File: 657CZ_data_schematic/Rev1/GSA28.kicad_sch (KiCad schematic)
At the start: 3 parts, among them J281P DA15_Socket, J281R DA15_Socket

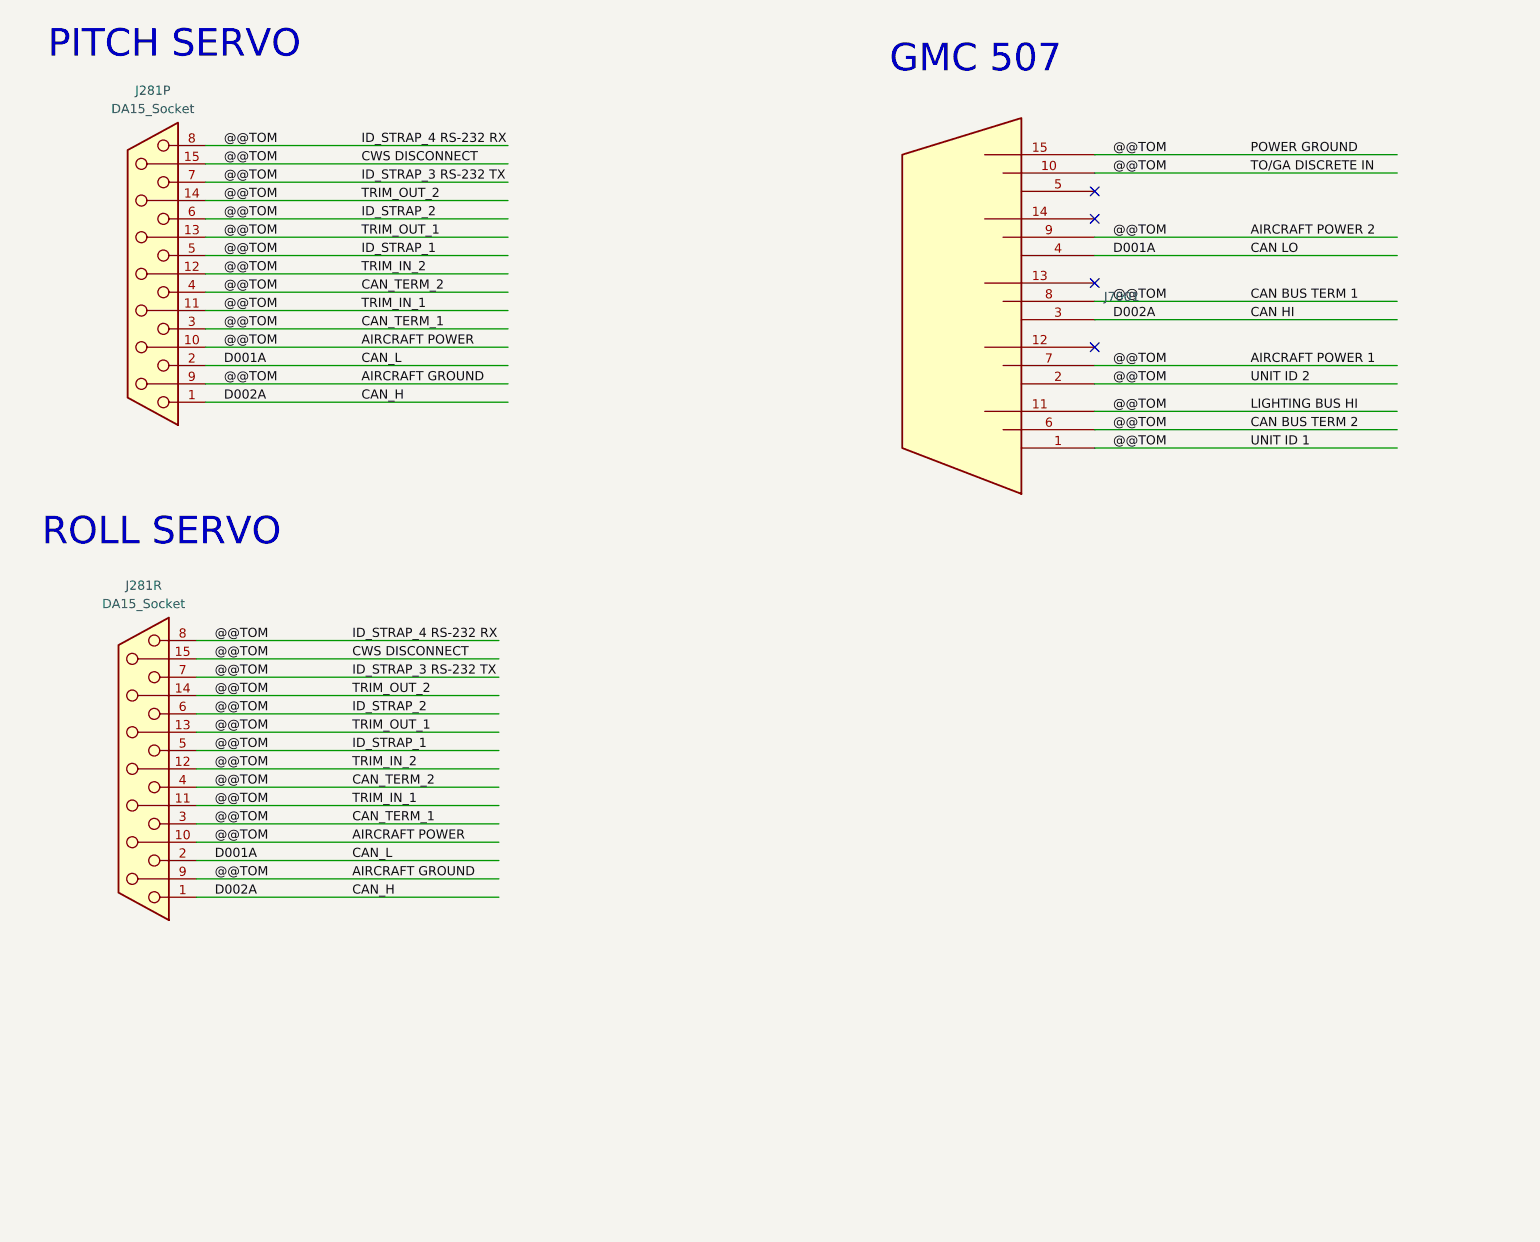
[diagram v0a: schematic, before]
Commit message: added data connections after AvClassics wiring. completed LRUs GMU, GDU, GSU, GAD, GNC, GTX, GTR  Not completed GMA, GEA and autopilot LRUs
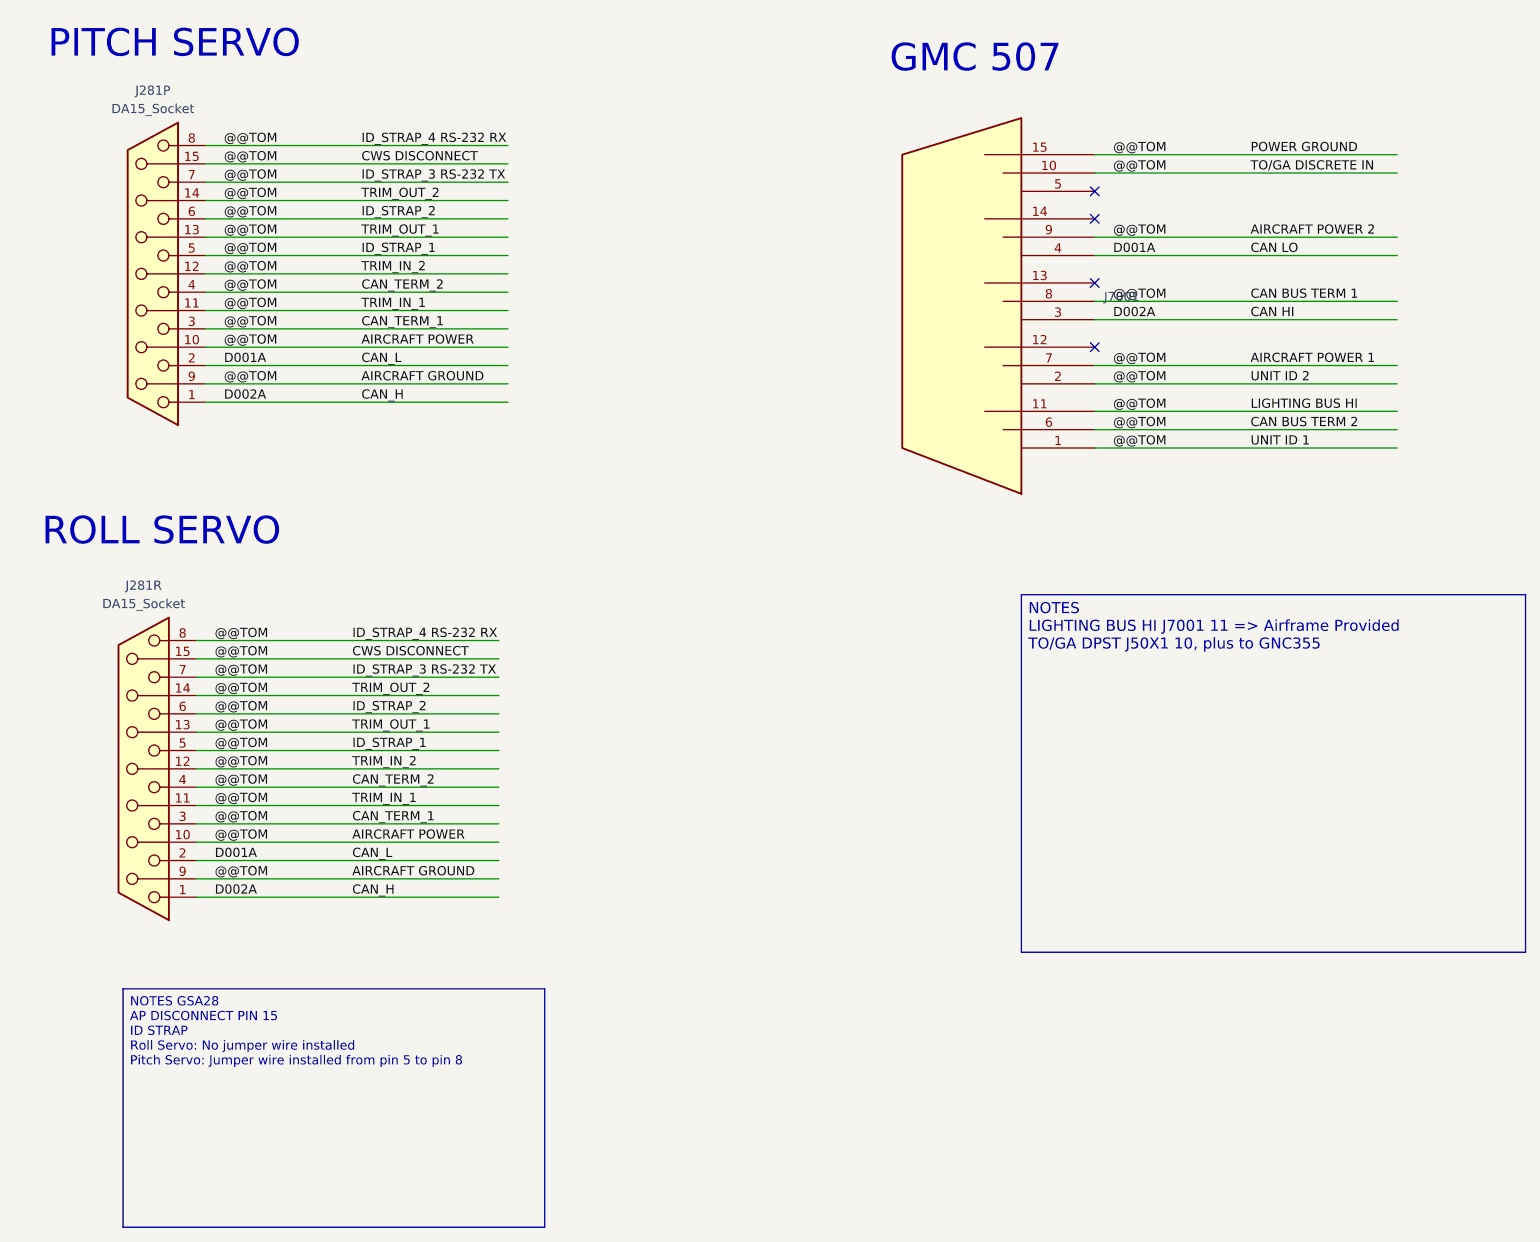
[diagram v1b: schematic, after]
